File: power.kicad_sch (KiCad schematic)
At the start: 32 parts, among them IC301 XL1509-5.0E1, IC302 SY8113BADC, Q301 AO3401A, Q302 AO3400A, Q303 AO3401A, Q304 AO3401A, SW301 1FS1T1B9M2RES-5, X301 KF2EDGR-3.81-3P

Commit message: start rework of baseboard.
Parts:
- renumbered C306 to C10, C307 to C11, C308 to C12, C309 to C13, C310 to C14, C311 to C15, C312 to C16, C301 to C5, C302 to C6, C303 to C7, C304 to C8, C305 to C9, D301 to D3, D302 to D4, D303 to D5, IC301 to IC3, IC302 to IC4, L301 to L1, L302 to L2, Q301 to Q1, Q302 to Q2, Q303 to Q3, Q304 to Q4, R301 to R3, R302 to R4, R303 to R5, R304 to R6, R305 to R7, R306 to R8, R307 to R9, SW301 to SW1, X301 to X5

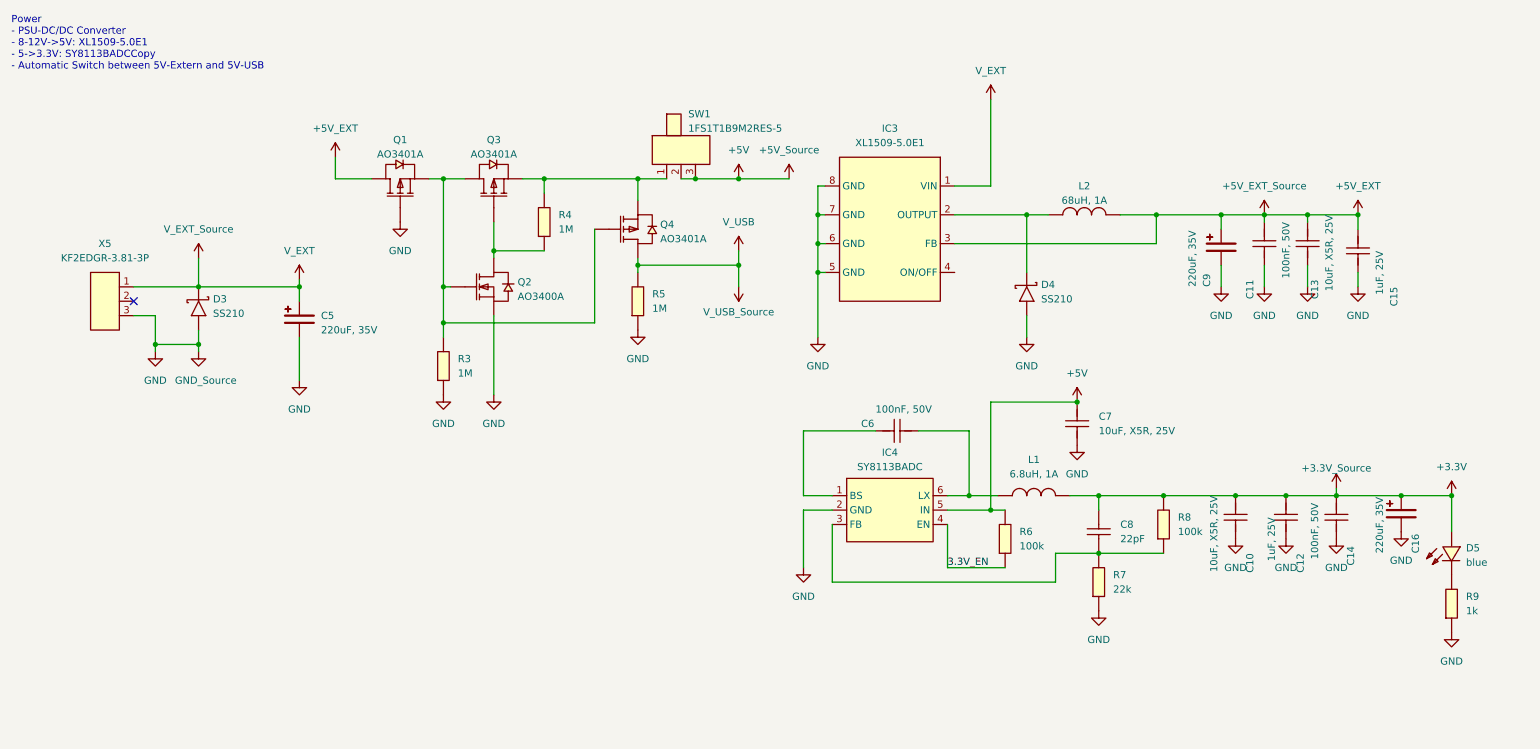
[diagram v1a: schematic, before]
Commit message: replace display with better module, start layout parts on pcb.
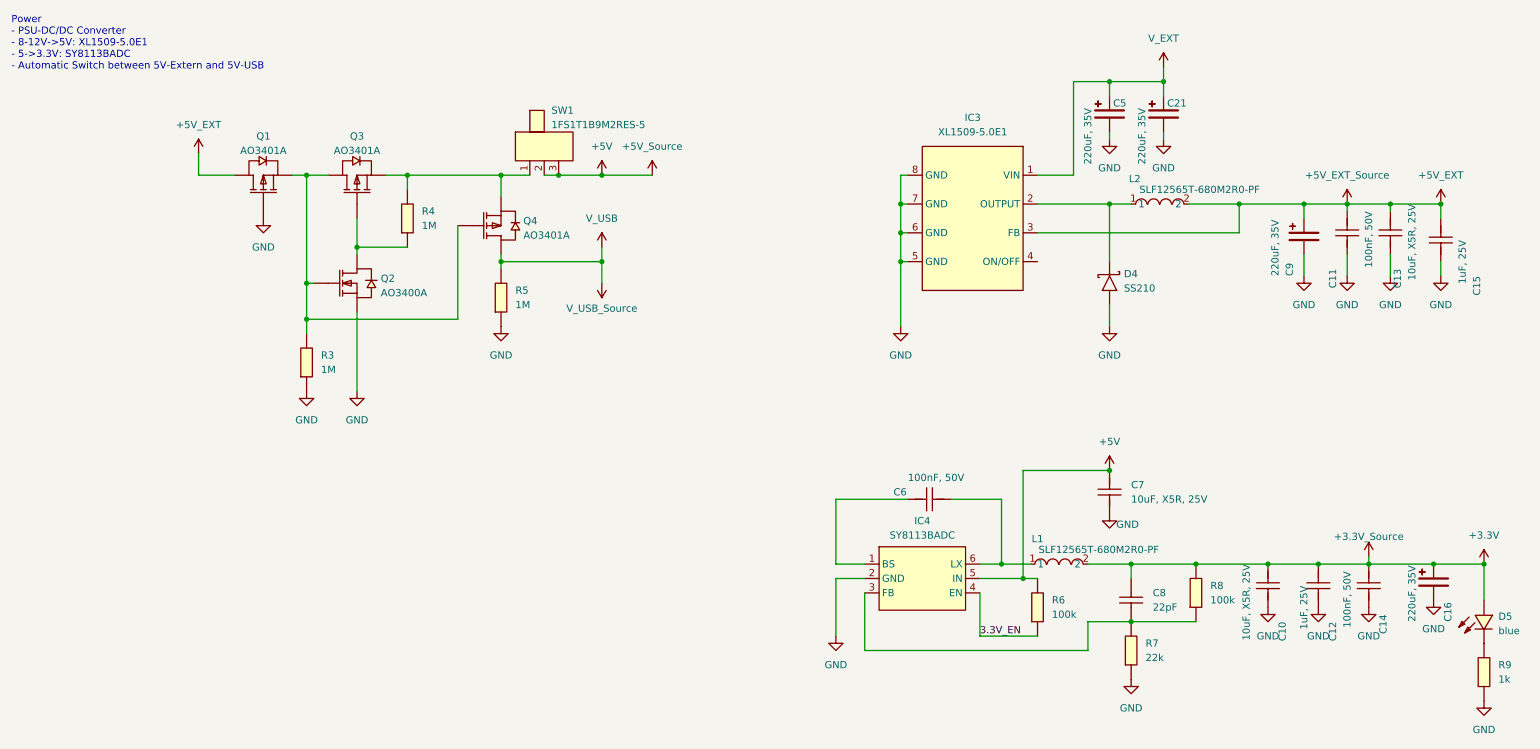
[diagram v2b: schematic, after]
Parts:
- removed D3: SS210, eduboardv2:SMA_L4.3-W2.6-LS5.2-RD, symbol eduboardv2:SS210
- removed L1: 6.8uH, 1A, eduboardv2:IND-SMD_L4.0-W4.0, symbol eduboardv2:SWPA4020S6R8MT
- removed L2: 68uH, 1A, eduboardv2:IND-SMD_L6.0-W6.0_FNR60XXS, symbol eduboardv2:SWPA6045S680MT
- removed X5: KF2EDGR-3.81-3P, eduboardv2:CONN-TH_3P-P3.81_KF2EDGR-3.81-3P, symbol eduboardv2:KF2EDGR-3.81-3P
- added C21: 220uF, 35V, EduboardV2_kicadlib:CAP-SMD_BD8.0-L8.3-W8.3-RD, symbol eduboardv2:VEJ221M1VTR-0810
- added L1, L2: SLF12565T-680M2R0-PF, EduboardV2_kicadlib:IND-SMD_L12.5-W12.5_SLF12565T, symbol EduboardV2_kicadlib:SLF12565T-680M2R0-PF
- C10, C13, C7: footprint eduboardv2:C0603 -> Capacitor_SMD:C_0603_1608Metric_Pad1.08x0.95mm_HandSolder
- C11, C12, C14, C15, C6, C8: footprint eduboardv2:C0402 -> Capacitor_SMD:C_0402_1005Metric_Pad0.74x0.62mm_HandSolder
- C16, C5, C9: footprint eduboardv2:CAP-SMD_BD8.0-L8.3-W8.3-RD -> EduboardV2_kicadlib:CAP-SMD_BD8.0-L8.3-W8.3-RD
- D4: footprint eduboardv2:SMA_L4.3-W2.6-LS5.2-RD -> EduboardV2_kicadlib:SMA_L4.3-W2.6-LS5.2-RD
- D5: footprint eduboardv2:LED0603-R-RD_BLUE -> EduboardV2_kicadlib:LED0603-FD_BLUE
- IC3: footprint eduboardv2:SOIC-8_L5.0-W4.0-P1.27-LS6.0-BL -> EduboardV2_kicadlib:SOIC-8_L5.0-W4.0-P1.27-LS6.0-BL
- IC4: footprint eduboardv2:TSOT-23-6_L2.9-W1.6-P0.95-LS2.8-BR -> EduboardV2_kicadlib:TSOT-23-6_L2.9-W1.6-P0.95-LS2.8-BR
- Q1, Q3, Q4: footprint eduboardv2:SOT-23_L2.9-W1.3-P1.90-LS2.4-BR -> EduboardV2_kicadlib:SOT-23_L2.9-W1.3-P1.90-LS2.4-BR
- Q2: footprint eduboardv2:SOT-23-3_L2.9-W1.6-P1.90-LS2.8-BR -> EduboardV2_kicadlib:SOT-23-3_L2.9-W1.6-P1.90-LS2.8-BR
- R3, R4, R5, R6, R7, R8, R9: footprint eduboardv2:R0402 -> Resistor_SMD:R_0402_1005Metric_Pad0.72x0.64mm_HandSolder
- SW1: footprint eduboardv2:SW-TH_1FS1T1B9M2RES-5 -> EduboardV2_kicadlib:SW-TH_1FS1T1B9M2RES-5
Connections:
- net +3.3V: now also L1.2
- net +5V_EXT: now also L2.2
- net GND: now also C21.2
- net V_EXT: now also C21.1
- net at C6.2, IC4.6 (LX): now also L1.1
- net at D4.1 (K), IC3.2 (OUTPUT): now also L2.1
- no-connect marks 1 -> 0
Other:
- note added: "Power - PSU-DC/DC Converter - 8-12V->5V: XL1509-5.0E1 - 5->3.3V: SY8113BADC - Automatic Switch between 5V-Extern and 5V-USB"
- note removed: "Power - PSU-DC/DC Converter - 8-12V->5V: XL1509-5.0E1 - 5->3.3V: SY8113BADCCopy - Automatic Switch between 5V-Extern and 5V-USB"
- moved on the sheet: C10, C11, C12, C13, C14, C15, C16, C6, C7, C8, C9, D4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

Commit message: Layout of parts done. Started laying tracks
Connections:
- net +3.3V: no longer C10.2, C12.1, C14.1, C16.1, C8.2, L1.2, R8.2
- new net: C10.2, C12.1, C14.1, C16.1, C8.2, L1.2, R8.2
- no-connect marks 0 -> 1
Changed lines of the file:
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@@
   (junction (at 83.82 42.545) (diameter 0) (color 0 0 0 0)
   )
-  (junction (at 264.795 111.125) (diameter 0) (color 0 0 0 0)
-  )
   (junction (at 118.11 57.785) (diameter 0) (color 0 0 0 0)
   )
-  (junction (at 273.685 111.125) (diameter 0) (color 0 0 0 0)
-  )
   (junction (at 207.645 26.035) (diameter 0) (color 0 0 0 0)
   )
@@
   (junction (at 207.645 94.615) (diameter 0) (color 0 0 0 0)
   )
+  (no_connect (at 194.945 57.785))
   (wire (pts (xy 170.815 57.785) (xy 170.815 69.215))
     (stroke (width 0) (type default))
@@
     (stroke (width 0) (type default))
   )
-  (wire (pts (xy 264.795 111.125) (xy 273.685 111.125))
-    (stroke (width 0) (type default))
-  )

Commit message: layout done so far. Have to check everything again
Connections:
- net +3.3V: now also C10.2, C12.1, C14.1, C16.1, C8.2, L1.2, R8.2
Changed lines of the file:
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@@
   (junction (at 211.455 121.285) (diameter 0) (color 0 0 0 0)
   )
+  (junction (at 273.685 111.125) (diameter 0) (color 0 0 0 0)
+  )
   (junction (at 207.645 94.615) (diameter 0) (color 0 0 0 0)
+  )
+  (junction (at 264.795 111.125) (diameter 0) (color 0 0 0 0)
   )
   (no_connect (at 194.945 57.785))
@@
     (stroke (width 0) (type default))
   )
+  (wire (pts (xy 264.795 111.125) (xy 273.685 111.125))
+    (stroke (width 0) (type default))
+  )

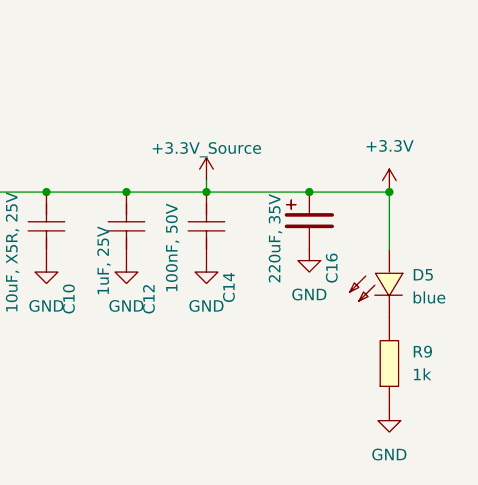
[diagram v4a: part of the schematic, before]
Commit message: fix parts (like led were wrong way round) Neatify Board
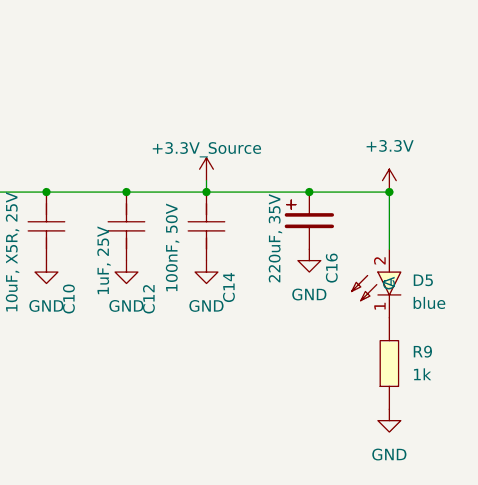
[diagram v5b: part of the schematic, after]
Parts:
- D5: symbol eduboardv2:19-217_BHC-ZL1M2RY_3T -> EduboardV2_kicadlib:19-217_BHC-ZL1M2RY_3T; Manufacturer EVERLIGHT -> EVERLIGHT(亿光)
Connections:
- net +3.3V: now also D5.2 (A); no longer D5.1 (A)
- net at R9.2: now also D5.1 (C); no longer D5.2 (C)
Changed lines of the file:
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@@
     )
   )
-  (symbol (lib_id "eduboardv2:19-217_BHC-ZL1M2RY_3T") (at 271.145 121.285 90) (unit 1)
+  (symbol (lib_id "EduboardV2_kicadlib:19-217_BHC-ZL1M2RY_3T") (at 271.78 121.285 90) (unit 1)
     (in_bom yes) (on_board yes) (dnp no) (fields_autoplaced)
-    (property "Reference" "D5" (at 276.225 120.3608 90)
+    (property "Reference" "D5" (at 276.225 120.9675 90)
       (effects (font (size 1.27 1.27)) (justify right))
     )
-    (property "Value" "blue" (at 276.225 122.9008 90)
+    (property "Value" "blue" (at 276.225 123.5075 90)
       (effects (font (size 1.27 1.27)) (justify right))
     )
-    (property "Footprint" "EduboardV2_kicadlib:LED0603-FD_BLUE" (at 280.795 121.285 0)
+    (property "Footprint" "EduboardV2_kicadlib:LED0603-FD_BLUE" (at 281.18 121.285 0)
       (effects (font (size 1.27 1.27)) hide)
     )
-    (property "Datasheet" "https://lcsc.com/product-detail/Light-Emitting-Diodes-LED_0603-Blue-light_C72041.html" (at 285.875 121.285 0)
+    (property "Datasheet" "https://lcsc.com/product-detail/Light-Emitting-Diodes-LED_0603-Blue-light_C72041.html" (at 283.72 121.285 0)
       (effects (font (size 1.27 1.27)) hide)
     )
-    (property "Manufacturer" "EVERLIGHT" (at 288.415 121.285 0)
+    (property "Manufacturer" "EVERLIGHT(亿光)" (at 286.26 121.285 0)
       (effects (font (size 1.27 1.27)) hide)
     )
-    (property "LCSC Part" "C72041" (at 290.955 121.285 0)
+    (property "LCSC Part" "C72041" (at 288.8 121.285 0)
       (effects (font (size 1.27 1.27)) hide)
     )
-    (property "JLC Part" "Basic Part" (at 293.495 121.285 0)
+    (property "JLC Part" "Basic Part" (at 291.34 121.285 0)
       (effects (font (size 1.27 1.27)) hide)
     )
-    (property "MPN" "19-217/BHC-ZL1M2RY/3T" (at 278.255 121.285 0)
+    (property "MPN" "19-217/BHC-ZL1M2RY/3T" (at 278.89 121.285 0)
       (effects (font (size 1.27 1.27)) hide)
     )

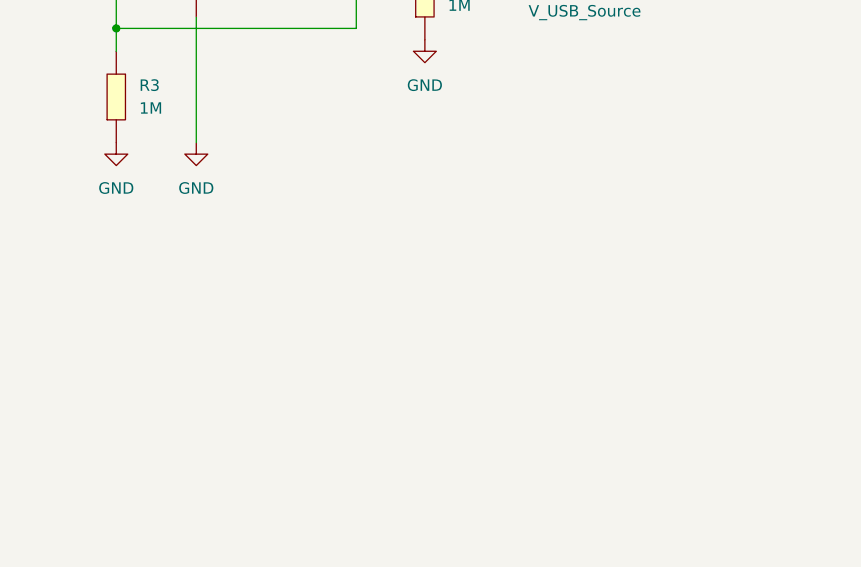
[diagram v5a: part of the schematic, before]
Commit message: mark errors found on first prototypes
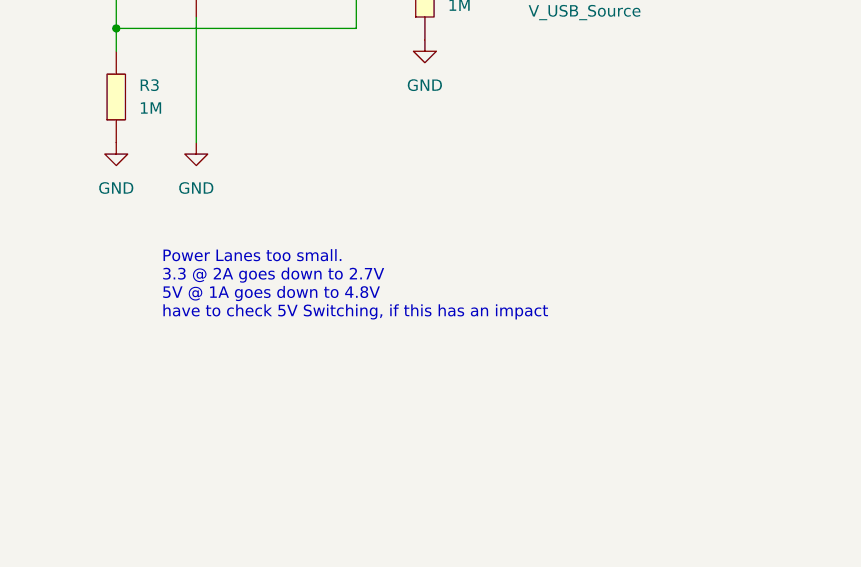
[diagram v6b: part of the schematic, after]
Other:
- note added: "Power Lanes too small. 3.3 @ 2A goes down to 2.7V 5V @ 1A goes down to 4.8V have to check 5V Switching, if this has an impact"
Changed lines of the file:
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@@
     (stroke (width 0) (type default))
+  )
+  (text "Power Lanes too small.\n3.3 @ 2A goes down to 2.7V\n5V @ 1A goes down to 4.8V\nhave to check 5V Switching, if this has an impact"
+    (at 71.12 100.33 0)
+    (effects (font (size 1.27 1.27) (color 255 0 0 1)) (justify left bottom))
   )
   (text "Power\n- PSU-DC/DC Converter\n- 8-12V->5V: XL1509-5.0E1\n- 5->3.3V: SY8113BADC\n- Automatic Switch between 5V-Extern and 5V-USB"

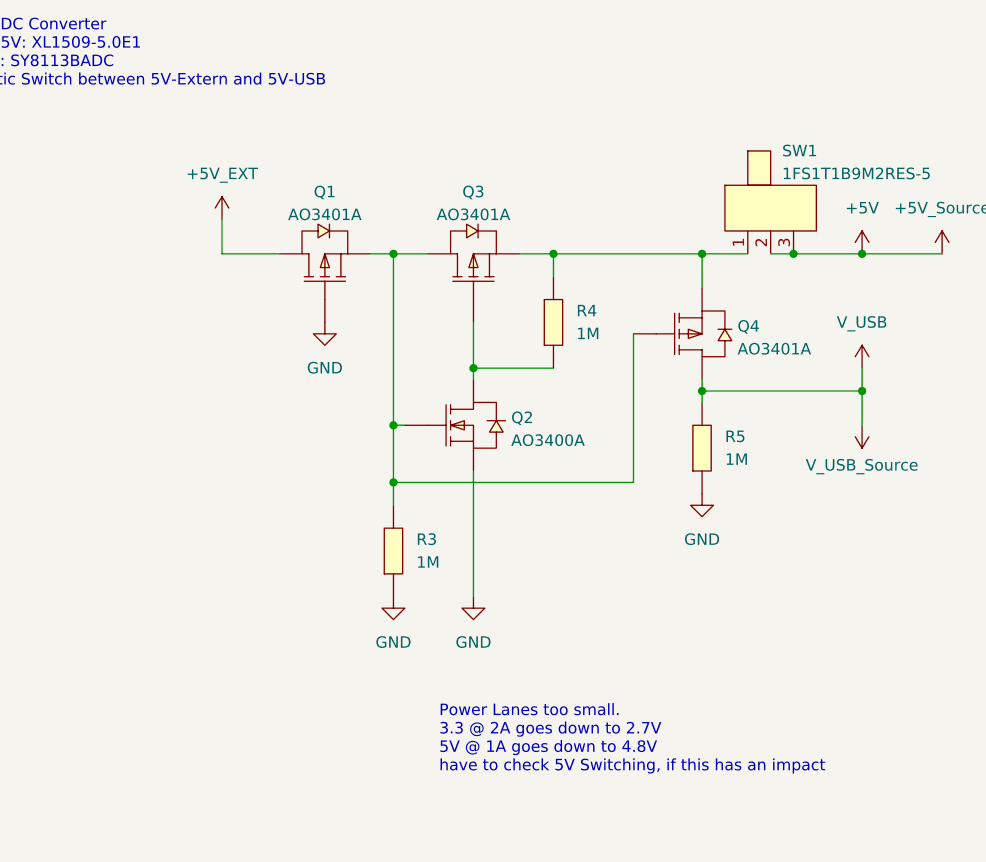
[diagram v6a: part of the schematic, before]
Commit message: change power switch fets to IRLML6402 and 2N7002
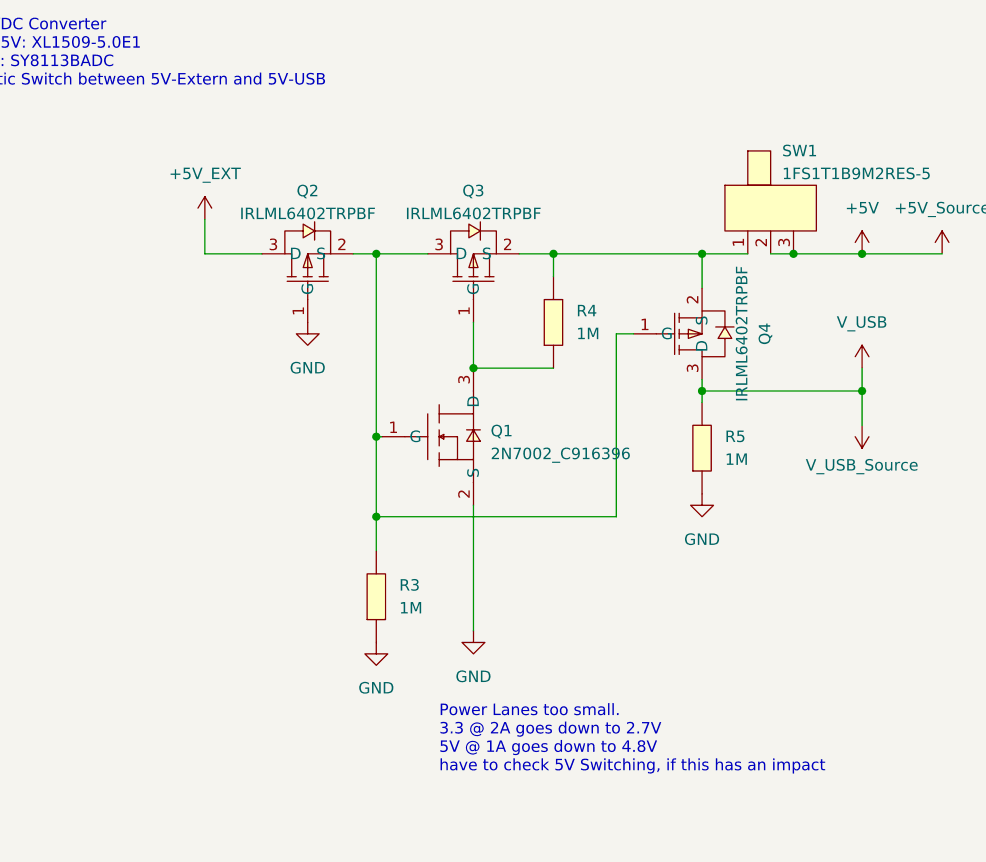
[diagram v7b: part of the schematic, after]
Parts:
- removed Q1, Q3, Q4: AO3401A, EduboardV2_kicadlib:SOT-23_L2.9-W1.3-P1.90-LS2.4-BR, symbol eduboardv2:AO3401A
- removed Q2: AO3400A, EduboardV2_kicadlib:SOT-23-3_L2.9-W1.6-P1.90-LS2.8-BR, symbol eduboardv2:AO3400A
- added Q1: 2N7002_C916396, EduboardV2_kicadlib:SOT-23-3_L2.9-W1.3-P1.90-LS2.4-BR, symbol EduboardV2_kicadlib:2N7002_C916396
- added Q2, Q3, Q4: IRLML6402TRPBF, EduboardV2_kicadlib:SOT-23-3_L2.9-W1.6-P1.90-LS2.8-BR, symbol EduboardV2_kicadlib:IRLML6402TRPBF
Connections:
- net +5V_EXT: now also Q2.3 (D)
- net GND: now also Q1.2 (S), Q2.1 (G)
- net V_USB: now also Q4.3 (D)
- net at R4.1: now also Q1.3 (D), Q3.1 (G)
- net at R4.2, SW1.1: now also Q3.2 (S), Q4.2 (S)
- net at R3.2: now also Q1.1 (G), Q2.2 (S), Q3.3 (D), Q4.1 (G)
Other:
- moved on the sheet: R3

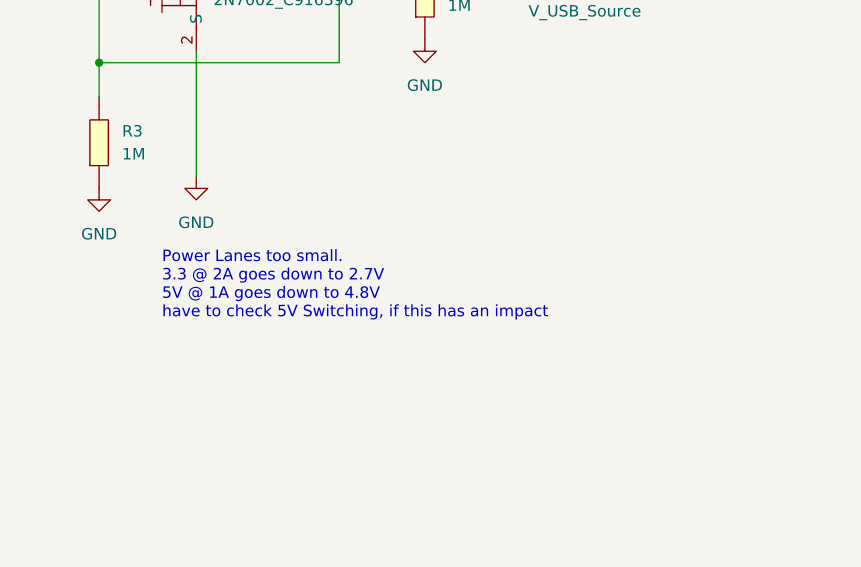
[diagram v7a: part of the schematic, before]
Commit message: Sort out RX/TX problems, improve DAC Circuits, Improve Board Text, switch out certain solder-jumpers with resistors
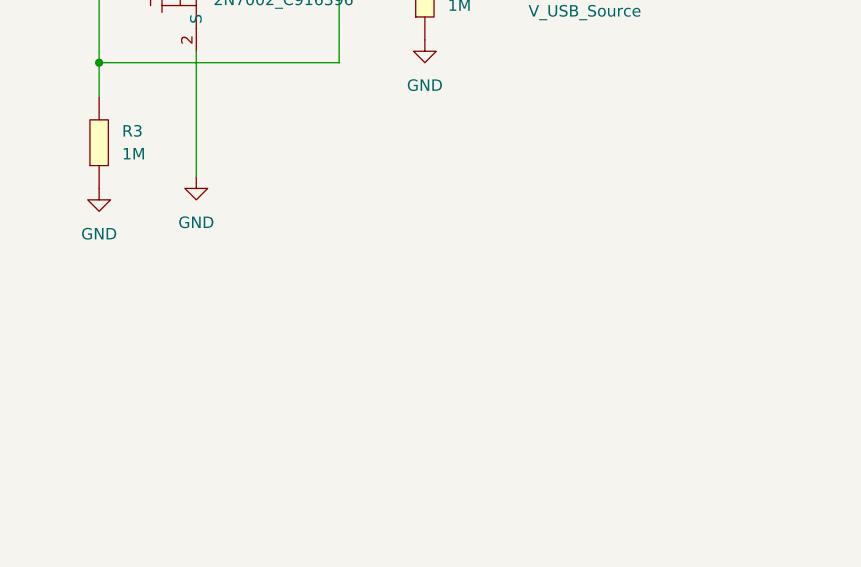
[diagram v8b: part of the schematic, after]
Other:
- note removed: "Power Lanes too small. 3.3 @ 2A goes down to 2.7V 5V @ 1A goes down to 4.8V have to check 5V Switching, if this has an impact"
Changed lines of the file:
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@@
     (stroke (width 0) (type default))
-  )
-  (text "Power Lanes too small.\n3.3 @ 2A goes down to 2.7V\n5V @ 1A goes down to 4.8V\nhave to check 5V Switching, if this has an impact"
-    (at 71.12 100.33 0)
-    (effects (font (size 1.27 1.27) (color 255 0 0 1)) (justify left bottom))
   )
   (text "Power\n- PSU-DC/DC Converter\n- 8-12V->5V: XL1509-5.0E1\n- 5->3.3V: SY8113BADC\n- Automatic Switch between 5V-Extern and 5V-USB"
